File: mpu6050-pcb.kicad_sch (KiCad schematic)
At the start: 9 parts, among them U1 MPU-6050

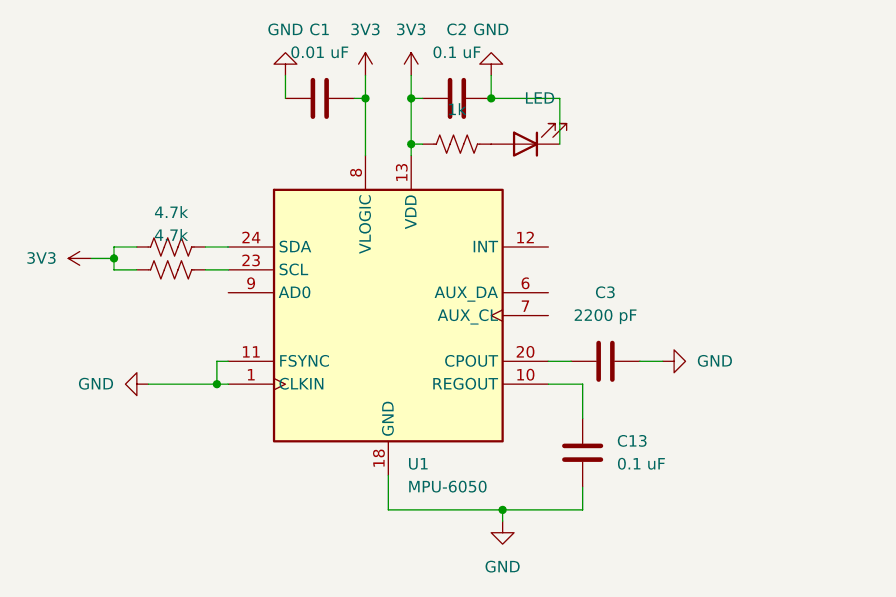
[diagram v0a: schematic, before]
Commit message: updated schematic and changed routing
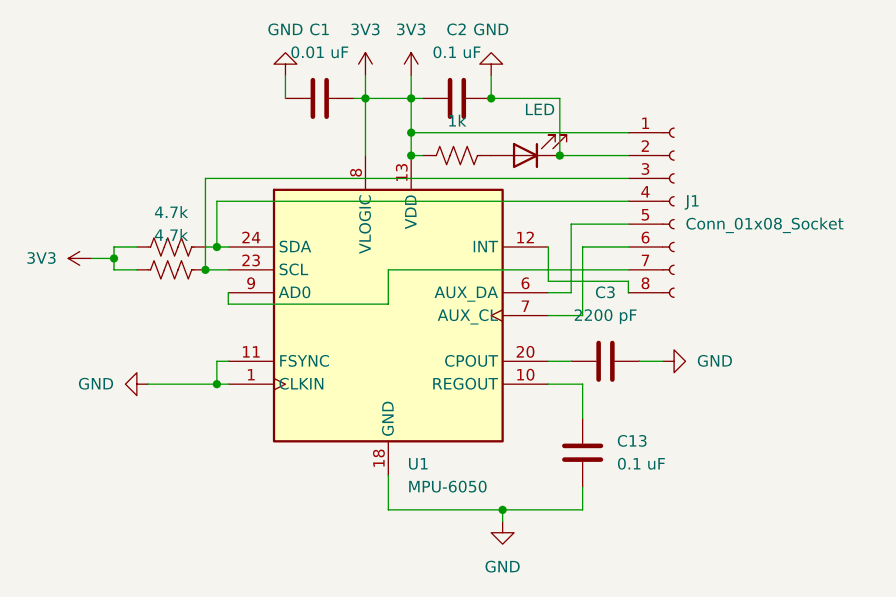
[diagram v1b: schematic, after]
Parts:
- added J1: Conn_01x08_Socket, Connector_PinSocket_2.54mm:PinSocket_1x08_P2.54mm_Vertical, symbol Connector:Conn_01x08_Socket
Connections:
- net 3V3: now also J1.1 (Pin_1)
- net GND: now also J1.2 (Pin_2)
- net at U1.12 (INT): now also J1.8 (Pin_8)
- net at R2.2, U1.23 (SCL): now also J1.3 (Pin_3)
- net at R1.2, U1.24 (SDA): now also J1.4 (Pin_4)
- net at U1.6 (AUX_DA): now also J1.5 (Pin_5)
- net at U1.7 (AUX_CL): now also J1.6 (Pin_6)
- net at U1.9 (AD0): now also J1.7 (Pin_7)

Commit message: changed routing and connector type
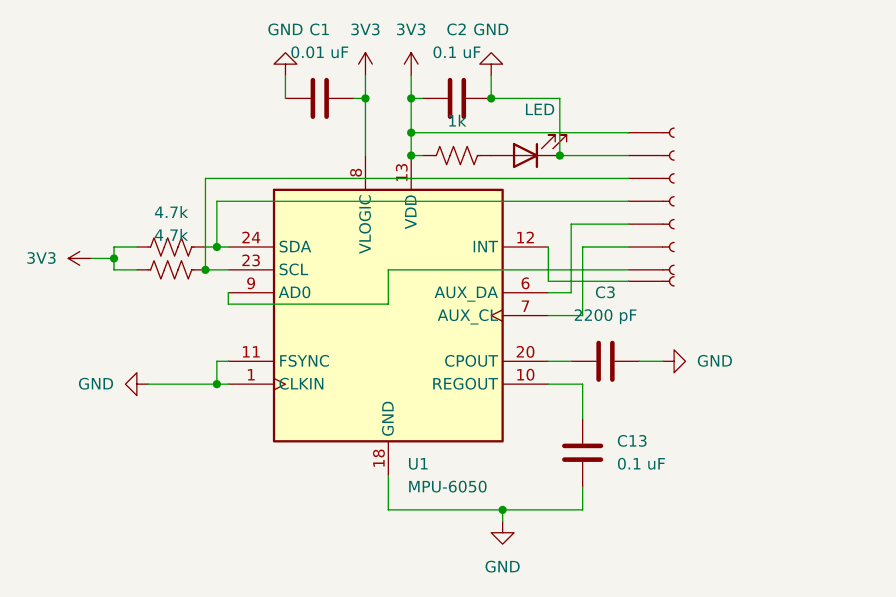
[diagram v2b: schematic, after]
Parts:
- removed J1: Conn_01x08_Socket, Connector_PinSocket_2.54mm:PinSocket_1x08_P2.54mm_Vertical, symbol Connector:Conn_01x08_Socket
- added J1, J2, J3, J4, J5, J6, J7, J8: Conn_01x01_Socket, Connector_PinSocket_2.54mm:PinSocket_1x01_P2.54mm_Vertical, symbol Connector:Conn_01x01_Socket
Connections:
- net 3V3: now also J2.1 (Pin_1)
- net GND: now also J1.1 (Pin_1)
- net at U1.12 (INT): now also J8.1 (Pin_1)
- net at R2.2, U1.23 (SCL): now also J3.1 (Pin_1)
- net at R1.2, U1.24 (SDA): now also J4.1 (Pin_1)
- net at U1.6 (AUX_DA): now also J5.1 (Pin_1)
- net at U1.7 (AUX_CL): now also J6.1 (Pin_1)
- net at U1.9 (AD0): now also J7.1 (Pin_1)
